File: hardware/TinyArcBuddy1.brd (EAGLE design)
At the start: 53.6 x 49.5 mm, 15 parts, among them IC1 ATTINY85ARCBUDDY

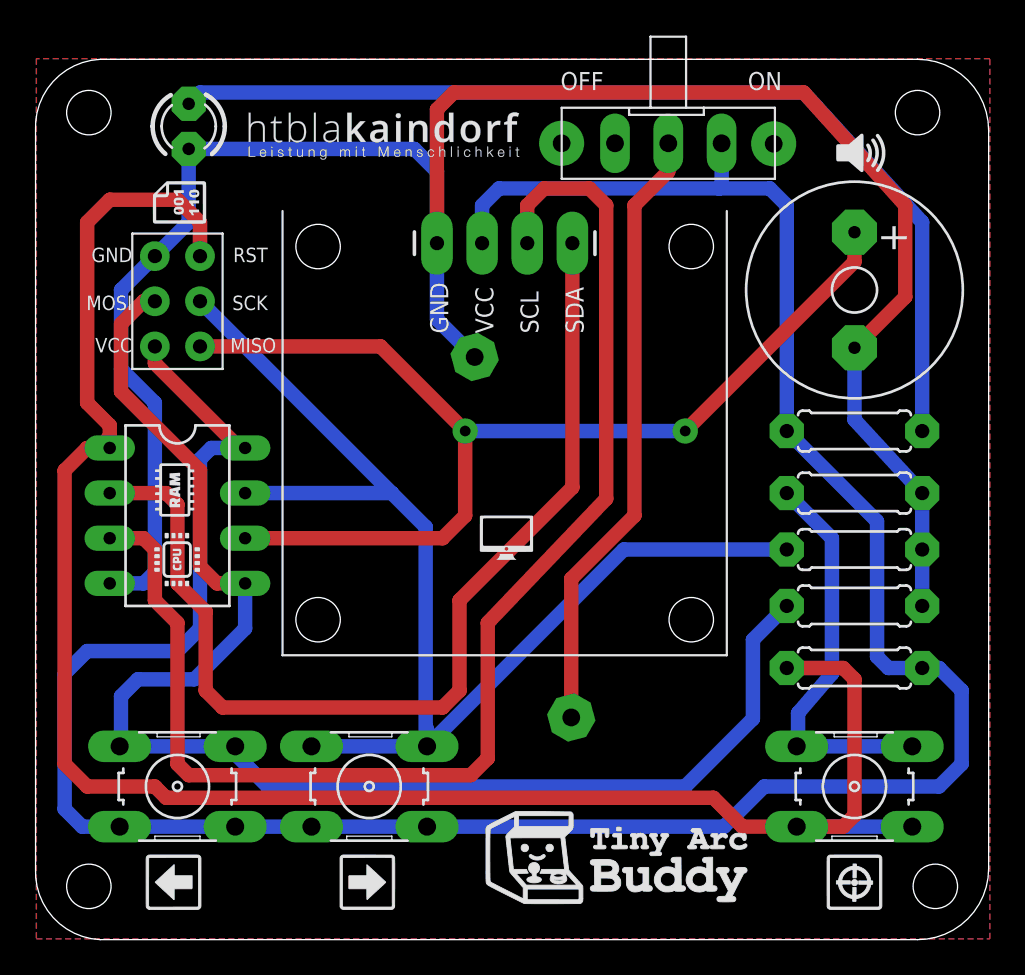
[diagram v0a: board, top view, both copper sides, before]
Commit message: increase drill diameters
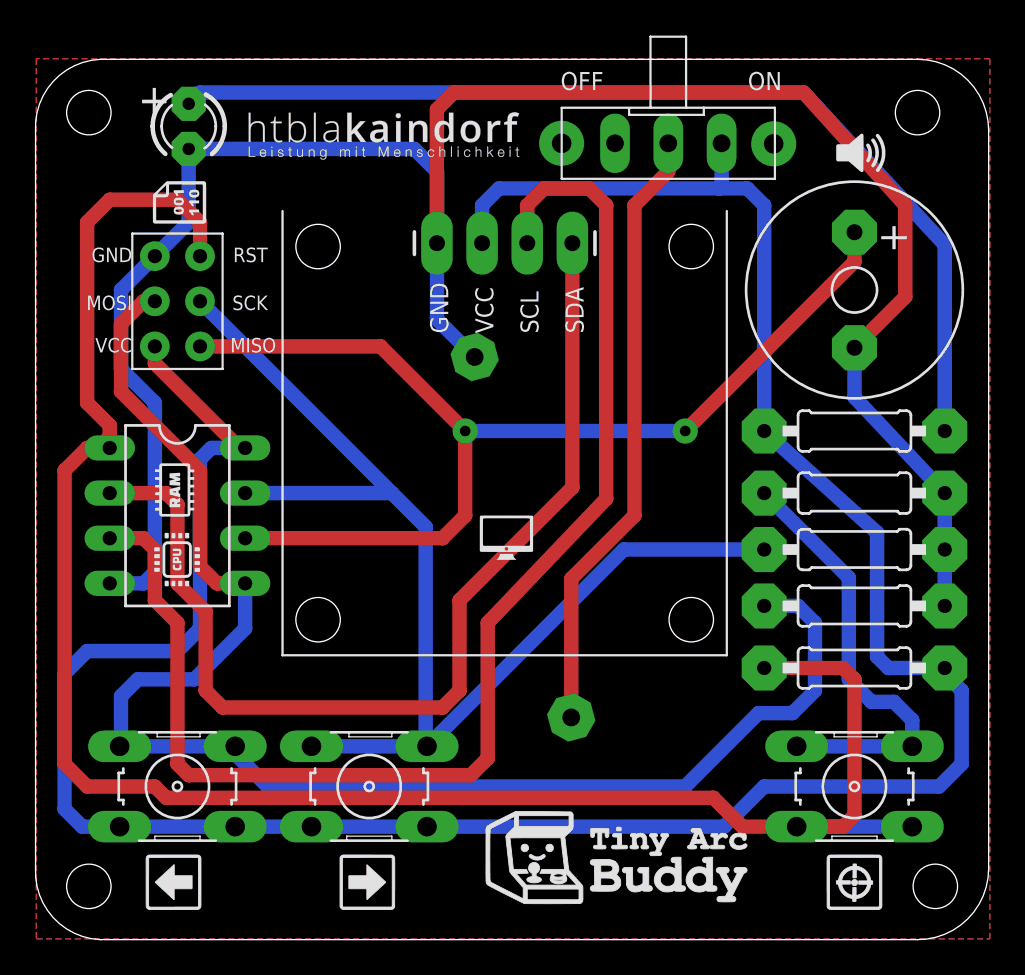
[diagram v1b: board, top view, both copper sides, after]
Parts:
- R1, R2, R3, R4, R5: device Kainduino:0207/7 -> Kainduino:0207/10
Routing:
- net MOSI: track 80.4 -> 84.4 mm
- net N$8: track 22.5 -> 25.1 mm
- net SCK: track 70.9 -> 68.7 mm
- net RESET: track 106.8 -> 108.1 mm
- net GND: track 117.3 -> 117.8 mm
- net N$4: track 56.5 -> 57.0 mm
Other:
- board text added: "+"
